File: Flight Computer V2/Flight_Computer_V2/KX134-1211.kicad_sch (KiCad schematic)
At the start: 4 parts, among them U4 KX134-1211

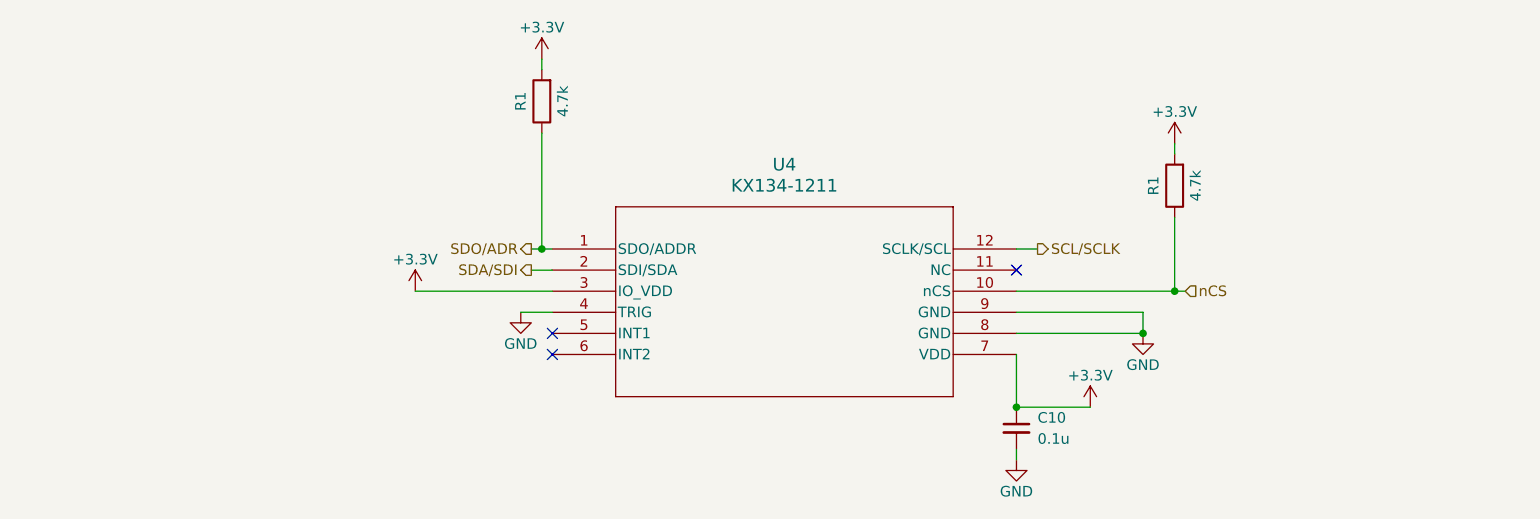
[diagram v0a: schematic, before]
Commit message: added more sensors to flight computer v2
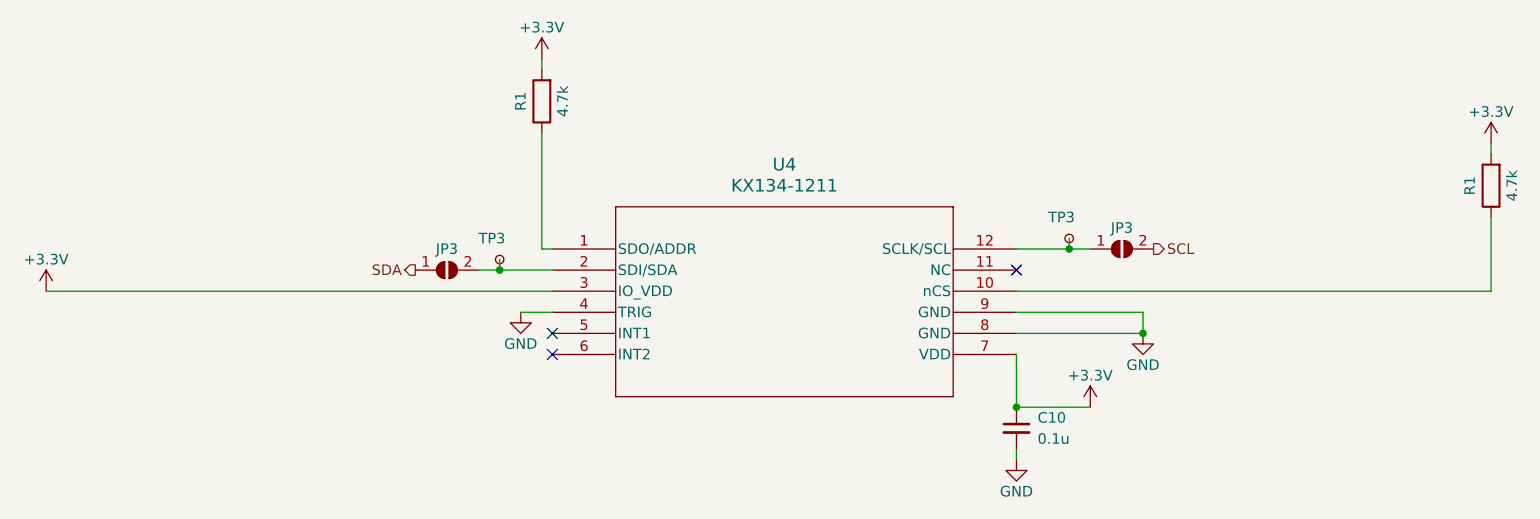
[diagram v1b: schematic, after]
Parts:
- added JP3 (x2): ~, symbol Jumper:SolderJumper_2_Open
- added TP3 (x2): TestPoint_Small, symbol Connector:TestPoint_Small
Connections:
- net SCL/SCLK: no longer names the net of U4.12 (SCLK/SCL)
- net SCL/SCLK: now also JP3.1 (A), TP3.1
- net SDA/SDI: no longer names the net of U4.2 (SDI/SDA)
- net SDA/SDI: now also JP3.2 (B), TP3.1
- net SDO/ADR: no longer names the net of R1.1, U4.1 (SDO/ADDR)
- net nCS: no longer names the net of R1.1, U4.10 (nCS)
- new net SCL: JP3.2 (B)
- new net SDA: JP3.1 (A)
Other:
- moved on the sheet: R1

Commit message: finalized schematic, added datasheets, and pdf of schematic
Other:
- company: (none) -> By: Dylan Haussecker
- title: (none) -> Avionics Flight Computer
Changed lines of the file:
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@@
 (kicad_sch (version 20230121) (generator eeschema)
   (paper "A4")
+  (title_block
+    (title "Avionics Flight Computer")
+    (date "2023-09-04")
+    (rev "1.0")
+    (company "By: Dylan Haussecker")
+  )
   (junction (at 115.57 80.01) (diameter 0) (color 0 0 0 0)
   )

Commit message: updated pcb
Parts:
- C10: footprint (none) -> Capacitor_SMD:C_0402_1005Metric
- JP3: footprint (none) -> Jumper:SolderJumper-2_P1.3mm_Open_Pad1.0x1.5mm
- R1: footprint (none) -> Resistor_SMD:R_0402_1005Metric
- TP3: footprint (none) -> TestPoint:TestPoint_Pad_D1.0mm
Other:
- moved on the sheet: U4
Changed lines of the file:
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@@
   (junction (at 177.8 96.52) (diameter 0) (color 0 0 0 0)
   )
-  (no_connect (at 177.8 80.01))
-  (no_connect (at 121.92 90.17))
-  (no_connect (at 121.92 87.63))
-  (wire (pts (xy 60.96 82.55) (xy 121.92 82.55))
-    (stroke (width 0) (type default))
-  )
-  (wire (pts (xy 177.8 87.63) (xy 193.04 87.63))
-    (stroke (width 0) (type default))
-  )
-  (wire (pts (xy 120.65 77.47) (xy 121.92 77.47))
+  (no_connect (at 175.26 81.28))
+  (no_connect (at 119.38 91.44))
+  (no_connect (at 119.38 88.9))
+  (wire (pts (xy 184.15 78.74) (xy 184.15 77.47))
+    (stroke (width 0) (type default))
+  )
+  (wire (pts (xy 119.38 83.82) (xy 119.38 82.55))
+    (stroke (width 0) (type default))
+  )
+  (wire (pts (xy 175.26 91.44) (xy 177.8 91.44))
+    (stroke (width 0) (type default))
+  )
+  (wire (pts (xy 175.26 88.9) (xy 180.34 88.9))
+    (stroke (width 0) (type default))
+  )
+  (wire (pts (xy 120.65 78.74) (xy 119.38 78.74))
+    (stroke (width 0) (type default))
+  )
+  (wire (pts (xy 119.38 82.55) (xy 60.96 82.55))
     (stroke (width 0) (type default))
   )
@@
     (stroke (width 0) (type default))
   )
-  (wire (pts (xy 177.8 77.47) (xy 184.15 77.47))
+  (wire (pts (xy 175.26 78.74) (xy 184.15 78.74))
+    (stroke (width 0) (type default))
+  )
+  (wire (pts (xy 118.11 86.36) (xy 118.11 85.09))
     (stroke (width 0) (type default))
   )
@@
     (stroke (width 0) (type default))
   )
-  (wire (pts (xy 177.8 90.17) (xy 177.8 96.52))
-    (stroke (width 0) (type default))
-  )
   (wire (pts (xy 184.15 77.47) (xy 186.69 77.47))
     (stroke (width 0) (type default))
   )
-  (wire (pts (xy 193.04 87.63) (xy 193.04 85.09))
+  (wire (pts (xy 115.57 81.28) (xy 115.57 80.01))
+    (stroke (width 0) (type default))
+  )
+  (wire (pts (xy 177.8 91.44) (xy 177.8 96.52))
+    (stroke (width 0) (type default))
+  )
+  (wire (pts (xy 193.04 87.63) (xy 193.04 86.36))
     (stroke (width 0) (type default))
   )
@@
     (stroke (width 0) (type default))
   )
-  (wire (pts (xy 115.57 80.01) (xy 121.92 80.01))
-    (stroke (width 0) (type default))
-  )
-  (wire (pts (xy 193.04 85.09) (xy 177.8 85.09))
-    (stroke (width 0) (type default))
-  )
-  (wire (pts (xy 118.11 85.09) (xy 121.92 85.09))
+  (wire (pts (xy 115.57 81.28) (xy 119.38 81.28))
+    (stroke (width 0) (type default))
+  )
+  (wire (pts (xy 180.34 87.63) (xy 193.04 87.63))
+    (stroke (width 0) (type default))
+  )
+  (wire (pts (xy 193.04 86.36) (xy 175.26 86.36))
+    (stroke (width 0) (type default))
+  )
+  (wire (pts (xy 118.11 86.36) (xy 119.38 86.36))
     (stroke (width 0) (type default))
   )
@@
     (stroke (width 0) (type default))
   )
-  (wire (pts (xy 120.65 63.5) (xy 120.65 77.47))
-    (stroke (width 0) (type default))
-  )
-  (wire (pts (xy 177.8 82.55) (xy 234.95 82.55))
+  (wire (pts (xy 120.65 63.5) (xy 120.65 78.74))
+    (stroke (width 0) (type default))
+  )
+  (wire (pts (xy 180.34 88.9) (xy 180.34 87.63))
+    (stroke (width 0) (type default))
+  )
+  (wire (pts (xy 175.26 83.82) (xy 234.95 83.82))
     (stroke (width 0) (type default))
   )
@@
     (stroke (width 0) (type default))
   )
-  (wire (pts (xy 234.95 73.66) (xy 234.95 82.55))
+  (wire (pts (xy 234.95 73.66) (xy 234.95 83.82))
     (stroke (width 0) (type default))
   )
@@
       (effects (font (size 1.27 1.27)) (justify left) hide)
     )
-    (property "Footprint" "" (at 120.65 78.74 0)
+    (property "Footprint" "TestPoint:TestPoint_Pad_D1.0mm" (at 120.65 78.74 0)
       (effects (font (size 1.27 1.27)) hide)
     )
@@
       (effects (font (size 1.27 1.27)))
     )
-    (property "Footprint" "" (at 109.22 80.01 0)
+    (property "Footprint" "Jumper:SolderJumper-2_P1.3mm_Open_Pad1.0x1.5mm" (at 109.22 80.01 0)
       (effects (font (size 1.27 1.27)) hide)
     )
@@
       (effects (font (size 1.27 1.27)))
     )
-    (property "Footprint" "" (at 190.5 77.47 0)
+    (property "Footprint" "Jumper:SolderJumper-2_P1.3mm_Open_Pad1.0x1.5mm" (at 190.5 77.47 0)
       (effects (font (size 1.27 1.27)) hide)
     )
@@
       (effects (font (size 1.27 1.27)))
     )
-    (property "Footprint" "" (at 236.728 69.85 90)
+    (property "Footprint" "Resistor_SMD:R_0402_1005Metric" (at 236.728 69.85 90)
       (effects (font (size 1.27 1.27)) hide)
     )
@@
       (effects (font (size 1.27 1.27)))
     )
-    (property "Footprint" "" (at 122.428 59.69 90)
+    (property "Footprint" "Resistor_SMD:R_0402_1005Metric" (at 122.428 59.69 90)
       (effects (font (size 1.27 1.27)) hide)
     )
@@
       (effects (font (size 1.27 1.27)) (justify left) hide)
     )
-    (property "Footprint" "" (at 189.23 76.2 0)
+    (property "Footprint" "TestPoint:TestPoint_Pad_D1.0mm" (at 189.23 76.2 0)
       (effects (font (size 1.27 1.27)) hide)
     )
@@
     )
   )
-  (symbol (lib_id "KX134-1211:KX134-1211") (at 121.92 77.47 0) (unit 1)
+  (symbol (lib_id "KX134-1211:KX134-1211") (at 119.38 78.74 0) (unit 1)
     (in_bom yes) (on_board yes) (dnp no) (fields_autoplaced)
-    (property "Reference" "U4" (at 149.86 67.31 0)
+    (property "Reference" "U4" (at 147.32 68.58 0)
       (effects (font (size 1.524 1.524)))
     )
-    (property "Value" "KX134-1211" (at 149.86 69.85 0)
+    (property "Value" "KX134-1211" (at 147.32 71.12 0)
       (effects (font (size 1.524 1.524)))
     )
-    (property "Footprint" "LGA12_2X2X0P9_ROM" (at 121.92 77.47 0)
+    (property "Footprint" "LGA12_2X2X0P9_ROM" (at 119.38 78.74 0)
       (effects (font (size 1.27 1.27) italic) hide)
     )
-    (property "Datasheet" "KX134-1211" (at 121.92 77.47 0)
+    (property "Datasheet" "KX134-1211" (at 119.38 78.74 0)
       (effects (font (size 1.27 1.27) italic) hide)
     )
@@
       (effects (font (size 1.27 1.27)) (justify left))
     )
-    (property "Footprint" "" (at 177.8 99.06 0)
-      (effects (font (size 1.27 1.27)) hide)
-    )
+    (property "Footprint" "Capacitor_SMD:C_0402_1005Metric" (at 177.8 99.06 0)
+      (effects (font (size 1.27 1.27)) hide)
+    )
